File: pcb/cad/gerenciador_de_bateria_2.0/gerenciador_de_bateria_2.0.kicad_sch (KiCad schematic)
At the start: 34 parts, among them J1 Conn_01x01_Female, J2 Conn_01x01_Female, J3 Conn_01x01_Female, J4 Conn_01x01_Female, J5 Conn_01x02_Male, J6 Conn_01x01_Female, J7 Conn_01x01_Female, SW1 SW_Push, U1 MP2731, U2 USB_BQ25629

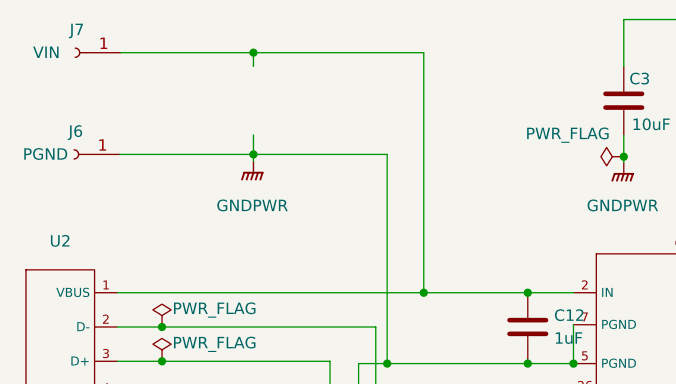
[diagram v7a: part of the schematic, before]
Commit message: Alterações no lauout de PCB do MP2731
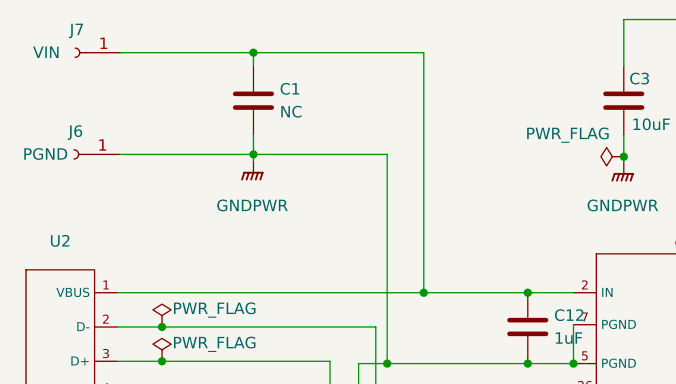
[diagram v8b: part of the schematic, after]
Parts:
- added C1: NC, Capacitor_SMD:C_0805_2012Metric, symbol Device:C
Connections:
- net GNDPWR: now also C1.2
- net at C12.1, J7.1 (Pin_1), U1.2 (IN)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: now also C1.1
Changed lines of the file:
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@@
+    (pin "2")
+  )
+  (symbol (lib_id "Device:C") (at 108.712 53.086 0) (unit 1)
+    (in_bom yes) (on_board yes) (fields_autoplaced)
+    (property "Reference" "C1" (id 0) (at 111.633 51.8159 0)
+      (effects (font (size 1.27 1.27)) (justify left))
+    )
+    (property "Value" "NC" (id 1) (at 111.633 54.3559 0)
+      (effects (font (size 1.27 1.27)) (justify left))
+    )
+    (property "Footprint" "Capacitor_SMD:C_0805_2012Metric" (id 2) (at 109.6772 56.896 0)
+      (effects (font (size 1.27 1.27)) hide)
+    )
+    (property "Datasheet" "~" (id 3) (at 108.712 53.086 0)
+      (effects (font (size 1.27 1.27)) hide)
+    )
+    (pin "1")
     (pin "2")
   )
@@
       (reference "#PWR0109") (unit 1) (value "GNDPWR") (footprint "")
     )
+    (path "/9de777ca-ce4f-4355-b350-be8705b17c42"
+      (reference "C1") (unit 1) (value "NC") (footprint "Capacitor_SMD:C_0805_2012Metric")
+    )
     (path "/9b755290-3e9c-4060-8937-1bc9c1c65b4b"
